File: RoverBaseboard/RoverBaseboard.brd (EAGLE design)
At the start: 87 x 62.9 mm, 61 parts, among them IC3 3.3V, U1 LD29150DT50R, U2 microSD

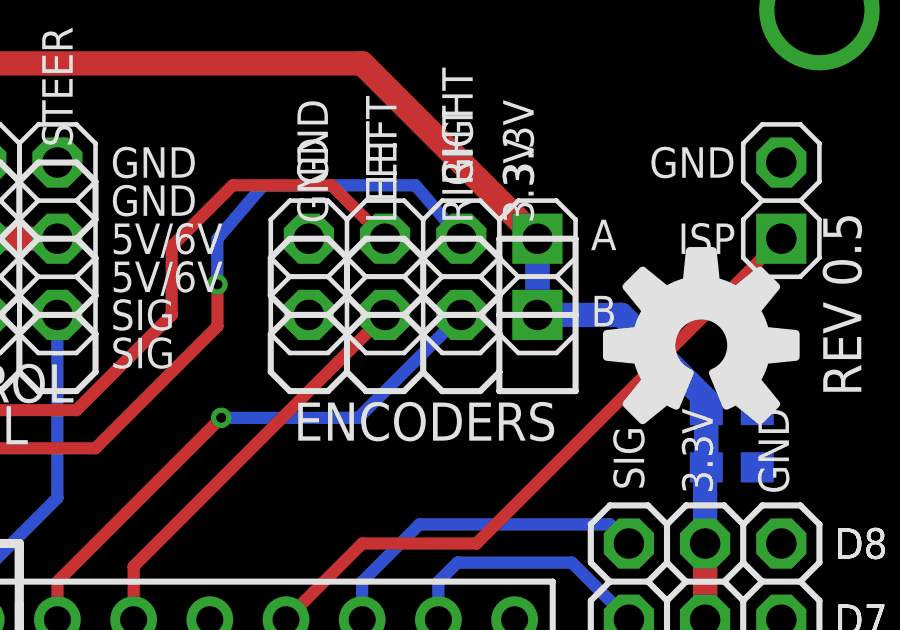
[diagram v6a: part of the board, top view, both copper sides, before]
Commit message: Revised net names to better reflect encoders. Changed pin header labels to better reflect function.
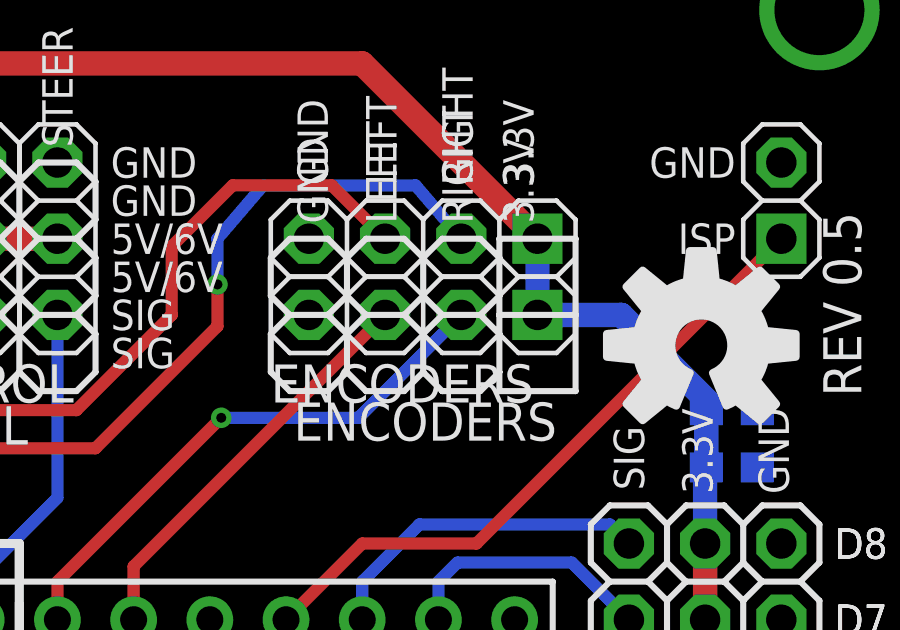
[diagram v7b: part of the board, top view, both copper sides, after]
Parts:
- JP1: value IO -> D0
- JP10: value PWM -> P1
- JP11: value PWM -> P2
- JP13: value IO -> D1
- JP14: value DIGITAL -> D2
- JP15: value ENCODERS -> A
- JP16: value ADC -> A0
- JP17: value ADC -> A1
- JP18: value ADC -> A2
- JP19: value ADC -> A3
- JP2: value ENCODERS -> B
- JP28: value DIGITAL -> D7
- JP29: value DIGITAL -> D8
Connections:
- net ENC0 renamed ENCA_LEFT
- net ENC1 renamed ENCA_RIGHT
- net ENC2 renamed ENCB_RIGHT
- net ENC3 renamed ENCB_LEFT
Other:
- board text removed: "A"
- board text removed: "B"
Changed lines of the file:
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@@
 <text x="11.938" y="45.339" size="1.27" layer="121" font="vector" ratio="16">I2C</text>
 <text x="7.62" y="20.574" size="1.27" layer="122" font="vector" ratio="16" rot="MR180">microSD</text>
-<text x="76.2" y="51.689" size="1.016" layer="25" font="vector" ratio="10">A</text>
-<text x="76.2" y="49.149" size="1.016" layer="25" font="vector" ratio="10">B</text>
 <text x="77.47" y="11.176" size="1.016" layer="25" ratio="10">ANALOG</text>
 <text x="77.47" y="23.876" size="1.016" layer="25" ratio="10">DIGITAL</text>
@@
 <text x="81.026" y="52.578" size="1.016" layer="25" font="vector" ratio="10" rot="R180">ISP</text>
 <text x="81.026" y="55.118" size="1.016" layer="25" font="vector" ratio="10" rot="R180">GND</text>
+<text x="65.532" y="46.609" size="1.27" layer="25" ratio="10">ENCODERS</text>
 </plain>
 <attributes>
@@
 <attribute name="NAME" x="8.255" y="51.054" size="1.016" layer="26" ratio="10" rot="MR270"/>
 </element>
-<element name="JP15" library="pinhead-2" package="1X04-S" value="ENCODERS" x="70.612" y="52.07" smashed="yes" rot="R180">
+<element name="JP15" library="pinhead-2" package="1X04-S" value="A" x="70.612" y="52.07" smashed="yes" rot="R180">
 <attribute name="OC_NEWARK" value="unknown" x="70.612" y="52.07" size="1.778" layer="27" rot="R180" display="off"/>
 <attribute name="MF" value="" x="70.612" y="52.07" size="1.778" layer="27" rot="R180" display="off"/>
 <attribute name="MPN" value="" x="70.612" y="52.07" size="1.778" layer="27" rot="R180" display="off"/>
+<attribute name="VALUE" x="76.2" y="51.435" size="1.016" layer="27"/>
 </element>
 <element name="JP4" library="pinhead-2" package="1X02-S" value="RST" x="19.05" y="6.35" smashed="yes">
@@
 <attribute name="NAME" x="62.992" y="11.938" size="1.016" layer="26" ratio="10" rot="MR90"/>
 </element>
-<element name="JP2" library="pinhead-2" package="1X04-S" value="ENCODERS" x="70.612" y="49.53" smashed="yes" rot="R180">
+<element name="JP2" library="pinhead-2" package="1X04-S" value="B" x="70.612" y="49.53" smashed="yes" rot="R180">
 <attribute name="OC_NEWARK" value="unknown" x="70.612" y="49.53" size="1.778" layer="27" rot="R180" display="off"/>
 <attribute name="MPN" value="" x="70.612" y="49.53" size="1.778" layer="27" rot="R180" display="off"/>
 <attribute name="MF" value="" x="70.612" y="49.53" size="1.778" layer="27" rot="R180" display="off"/>
-<attribute name="VALUE" x="66.294" y="46.609" size="1.27" layer="27" font="vector" ratio="10"/>
+<attribute name="VALUE" x="76.2" y="48.895" size="1.016" layer="27"/>
 </element>
 <element name="JP5" library="pinhead-2" package="1X03-S" value="RXSPD" x="50.8" y="52.07" smashed="yes" rot="R90">
@@
 <attribute name="VALUE" x="53.594" y="56.388" size="1.016" layer="27" font="vector" ratio="10" rot="R90"/>
 </element>
-<element name="JP10" library="pinhead-2" package="1X03-S" value="PWM" x="80.01" y="34.29" smashed="yes">
+<element name="JP10" library="pinhead-2" package="1X03-S" value="P1" x="80.01" y="34.29" smashed="yes">
 <attribute name="OC_NEWARK" value="unknown" x="80.01" y="34.29" size="1.778" layer="27" display="off"/>
 <attribute name="MPN" value="" x="80.01" y="34.29" size="1.778" layer="27" display="off"/>
 <attribute name="MF" value="" x="80.01" y="34.29" size="1.778" layer="27" display="off"/>
 </element>
-<element name="JP11" library="pinhead-2" package="1X03-S" value="PWM" x="80.01" y="36.83" smashed="yes">
+<element name="JP11" library="pinhead-2" package="1X03-S" value="P2" x="80.01" y="36.83" smashed="yes">
 <attribute name="OC_NEWARK" value="unknown" x="80.01" y="36.83" size="1.778" layer="27" display="off"/>
 <attribute name="MPN" value="" x="80.01" y="36.83" size="1.778" layer="27" display="off"/>
 <attribute name="MF" value="" x="80.01" y="36.83" size="1.778" layer="27" display="off"/>
 </element>
-<element name="JP1" library="pinhead-2" package="1X03-S" value="IO" x="80.01" y="31.75" smashed="yes">
+<element name="JP1" library="pinhead-2" package="1X03-S" value="D0" x="80.01" y="31.75" smashed="yes">
 <attribute name="OC_NEWARK" value="unknown" x="80.01" y="31.75" size="1.016" layer="27" font="vector" ratio="12" display="off"/>
 <attribute name="MPN" value="" x="80.01" y="31.75" size="1.016" layer="27" font="vector" ratio="12" display="off"/>
 <attribute name="MF" value="" x="80.01" y="31.75" size="1.016" layer="27" font="vector" ratio="12" display="off"/>
 </element>
-<element name="JP13" library="pinhead-2" package="1X03-S" value="IO" x="80.01" y="29.21" smashed="yes">
+<element name="JP13" library="pinhead-2" package="1X03-S" value="D1" x="80.01" y="29.21" smashed="yes">
 <attribute name="OC_NEWARK" value="unknown" x="80.01" y="29.21" size="1.016" layer="27" font="vector" ratio="12" display="off"/>
 <attribute name="MPN" value="" x="80.01" y="29.21" size="1.016" layer="27" font="vector" ratio="12" display="off"/>
 <attribute name="MF" value="" x="80.01" y="29.21" size="1.016" layer="27" font="vector" ratio="12" display="off"/>
 </element>
-<element name="JP14" library="pinhead-2" package="1X03-S" value="DIGITAL" x="80.01" y="26.67" smashed="yes">
+<element name="JP14" library="pinhead-2" package="1X03-S" value="D2" x="80.01" y="26.67" smashed="yes">
 <attribute name="OC_NEWARK" value="unknown" x="80.01" y="26.67" size="1.016" layer="27" font="vector" ratio="12" display="off"/>
 <attribute name="MPN" value="" x="80.01" y="26.67" size="1.016" layer="27" font="vector" ratio="12" display="off"/>
@@
 <attribute name="VALUE" x="74.295" y="22.225" size="1.27" layer="21" ratio="10" rot="R90"/>
 </element>
-<element name="JP16" library="pinhead-2" package="1X03-S" value="ADC" x="80.01" y="21.59" smashed="yes">
+<element name="JP16" library="pinhead-2" package="1X03-S" value="A0" x="80.01" y="21.59" smashed="yes">
 <attribute name="OC_NEWARK" value="unknown" x="80.01" y="21.59" size="1.016" layer="27" font="vector" ratio="12" display="off"/>
 <attribute name="MPN" value="" x="80.01" y="21.59" size="1.016" layer="27" font="vector" ratio="12" display="off"/>
 <attribute name="MF" value="" x="80.01" y="21.59" size="1.016" layer="27" font="vector" ratio="12" display="off"/>
 </element>
-<element name="JP17" library="pinhead-2" package="1X03-S" value="ADC" x="80.01" y="19.05" smashed="yes">
+<element name="JP17" library="pinhead-2" package="1X03-S" value="A1" x="80.01" y="19.05" smashed="yes">
 <attribute name="OC_NEWARK" value="unknown" x="80.01" y="19.05" size="1.016" layer="27" font="vector" ratio="12" display="off"/>
 <attribute name="MPN" value="" x="80.01" y="19.05" size="1.016" layer="27" font="vector" ratio="12" display="off"/>
 <attribute name="MF" value="" x="80.01" y="19.05" size="1.016" layer="27" font="vector" ratio="12" display="off"/>
 </element>
-<element name="JP18" library="pinhead-2" package="1X03-S" value="ADC" x="80.01" y="16.51" smashed="yes">
+<element name="JP18" library="pinhead-2" package="1X03-S" value="A2" x="80.01" y="16.51" smashed="yes">
 <attribute name="OC_NEWARK" value="unknown" x="80.01" y="16.51" size="1.016" layer="27" font="vector" ratio="12" display="off"/>
 <attribute name="MPN" value="" x="80.01" y="16.51" size="1.016" layer="27" font="vector" ratio="12" display="off"/>
 <attribute name="MF" value="" x="80.01" y="16.51" size="1.016" layer="27" font="vector" ratio="12" display="off"/>
 </element>
-<element name="JP19" library="pinhead-2" package="1X03-S" value="ADC" x="80.01" y="13.97" smashed="yes">
+<element name="JP19" library="pinhead-2" package="1X03-S" value="A3" x="80.01" y="13.97" smashed="yes">
 <attribute name="OC_NEWARK" value="unknown" x="80.01" y="13.97" size="1.016" layer="27" font="vector" ratio="12" display="off"/>
 <attribute name="MPN" value="" x="80.01" y="13.97" size="1.016" layer="27" font="vector" ratio="12" display="off"/>
 <attribute name="MF" value="" x="80.01" y="13.97" size="1.016" layer="27" font="vector" ratio="12" display="off"/>
 </element>
-<element name="JP28" library="pinhead-2" package="1X03-S" value="DIGITAL" x="80.01" y="39.37" smashed="yes">
+<element name="JP28" library="pinhead-2" package="1X03-S" value="D7" x="80.01" y="39.37" smashed="yes">
 <attribute name="OC_NEWARK" value="unknown" x="80.01" y="39.37" size="1.6764" layer="27" font="vector" ratio="12" display="off"/>
 <attribute name="MPN" value="" x="80.01" y="39.37" size="1.6764" layer="27" font="vector" ratio="12" display="off"/>
 <attribute name="MF" value="" x="80.01" y="39.37" size="1.6764" layer="27" font="vector" ratio="12" display="off"/>
 </element>
-<element name="JP29" library="pinhead-2" package="1X03-S" value="DIGITAL" x="80.01" y="41.91" smashed="yes">
+<element name="JP29" library="pinhead-2" package="1X03-S" value="D8" x="80.01" y="41.91" smashed="yes">
 <attribute name="OC_NEWARK" value="unknown" x="80.01" y="41.91" size="1.6764" layer="27" font="vector" ratio="12" display="off"/>
 <attribute name="MPN" value="" x="80.01" y="41.91" size="1.6764" layer="27" font="vector" ratio="12" display="off"/>
@@
 <wire x1="63.5" y1="6.35" x2="63.5" y2="9.31" width="0.4064" layer="16"/>
 </signal>
-<signal name="ENC2">
+<signal name="ENCB_RIGHT">
 <contactref element="JP2" pad="2"/>
 <contactref element="U$1" pad="J6-48"/>
@@
 <wire x1="68.453" y1="46.101" x2="71.882" y2="49.53" width="0.4064" layer="16"/>
 </signal>
-<signal name="ENC3">
+<signal name="ENCB_LEFT">
 <contactref element="JP2" pad="3"/>
 <contactref element="U$1" pad="J6-49"/>
@@
 <wire x1="66.04" y1="36.918" x2="66.04" y2="39.37" width="0.4064" layer="1"/>
 </signal>
-<signal name="ENC0">
+<signal name="ENCA_LEFT">
 <contactref element="U$1" pad="J6-38"/>
 <wire x1="37.465" y1="46.355" x2="33.02" y2="41.91" width="0.4064" layer="1"/>
@@
 <wire x1="67.564" y1="53.848" x2="69.342" y2="52.07" width="0.4064" layer="1"/>
 </signal>
-<signal name="ENC1">
+<signal name="ENCA_RIGHT">
 <contactref element="U$1" pad="J6-39"/>
 <contactref element="JP15" pad="2"/>

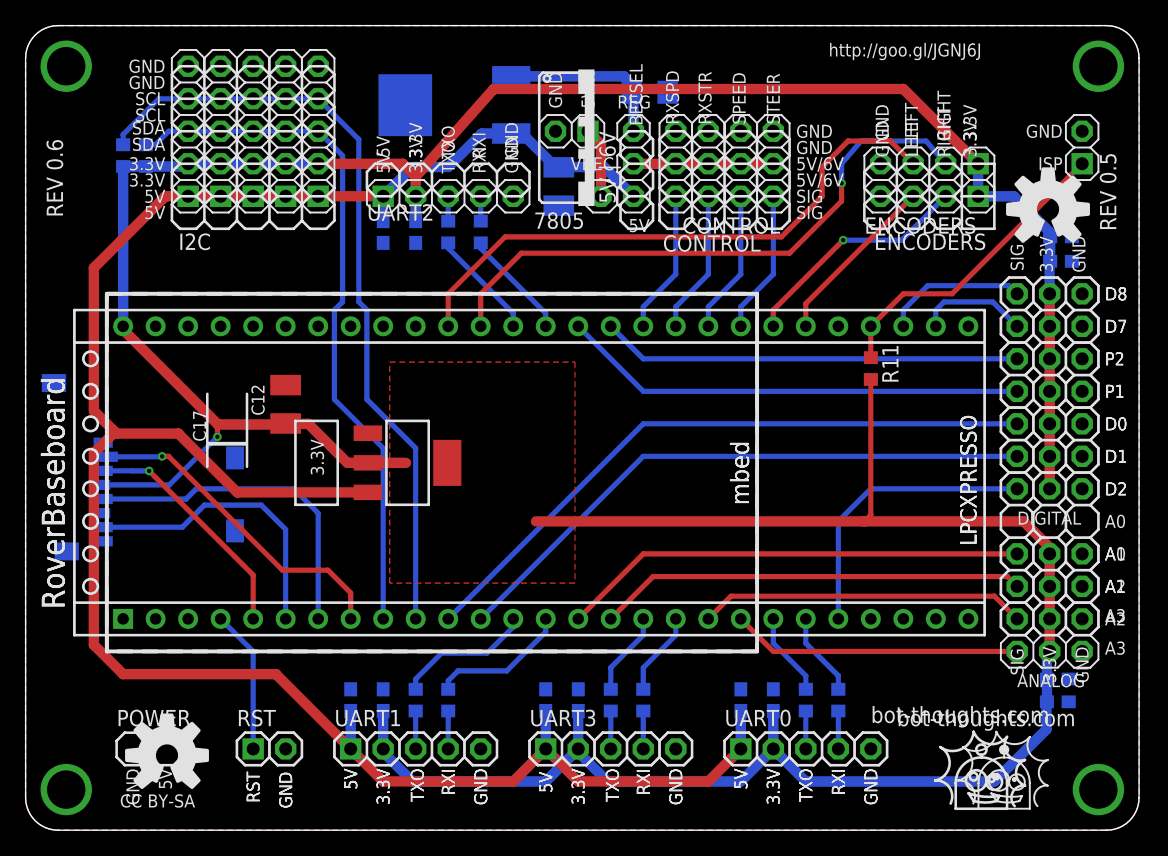
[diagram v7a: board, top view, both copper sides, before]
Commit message: Updated pin names, removed BEC>5V regulator, moved VIN pins back to original spot.
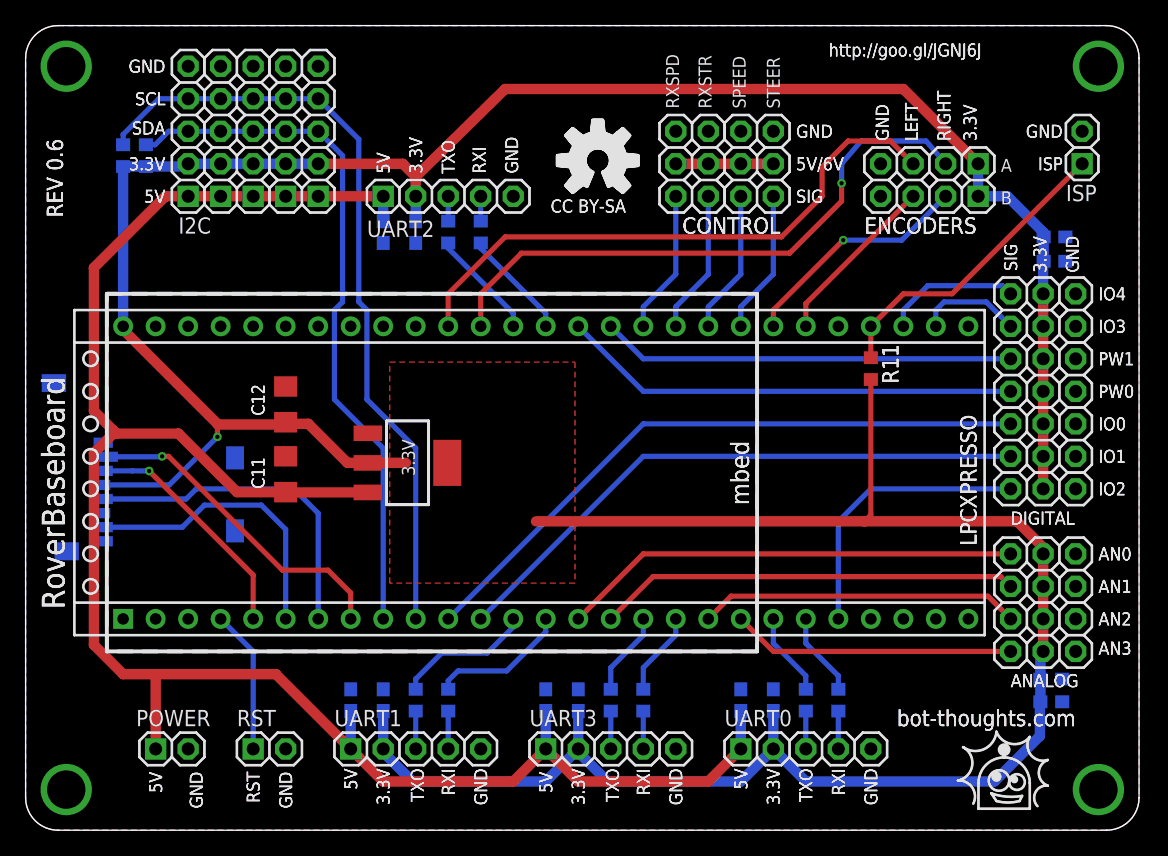
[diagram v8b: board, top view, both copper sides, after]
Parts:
- removed BEC: REG | BYP | 5VIN, pinhead-2:1X03-S
- removed C10: 106, rcl:C1206
- removed JP12: 5VIN, pinhead-2:1X01-S
- removed U1: LD29150DT50R, bt_regulator:DPAK
- C11, C12: value 33uF -> 10uF; device rcl:SMC_B -> rcl:C1206
- JP3: value PWR -> POWER
- moved JP3 57.5 mm to (11.4, 6.35), turned to 0 degrees
- moved C11 31.0 mm to (20.3, 27.8), flipped to the top, turned to 90 degrees
- moved JP1 0.51 mm to (79.5, 31.8)
- moved JP10 0.51 mm to (79.5, 34.3)
- moved JP11 0.51 mm to (79.5, 36.8)
- moved JP13 0.51 mm to (79.5, 29.2)
- moved JP14 0.51 mm to (79.5, 26.7)
- moved JP16 0.51 mm to (79.5, 21.6)
- moved JP17 0.51 mm to (79.5, 19.1)
- moved JP18 0.51 mm to (79.5, 16.5)
- moved JP19 0.51 mm to (79.5, 14.0)
- moved JP28 0.51 mm to (79.5, 39.4)
- moved JP29 0.51 mm to (79.5, 41.9)
- moved C20 0.51 mm to (80.1, 11.8)
- moved C21 0.51 mm to (80.1, 10.0)
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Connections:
- net D0 renamed P11
- net D1 renamed P12
- removed net 5VIN: JP12.1, JP3.1
- removed net 6-7V: BEC.1, C10.1, U1.1
- net +3V3: now also C12.1; no longer C12.+
- net +5V: now also C11.1, JP3.1; no longer BEC.3, C11.+, U1.3
- net BEC: no longer BEC.2
- net GND: now also C11.2, C12.2; no longer C10.2, C11.-, C12.-, U1.4
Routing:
- net +5V: track 170.1 -> 152.4 mm
- net 6-7V: track 13.6 -> 0.00 mm
- net 5VIN: track 5.50 -> 0.00 mm
- net BEC: track 10.9 -> 7.62 mm
- net +3V3: track 291.2 -> 289.8 mm
- net PWM2: track 32.8 -> 32.3 mm
- net PWM1: track 36.4 -> 35.9 mm
- net P12: track 47.2 -> 46.7 mm
- net P11: track 50.8 -> 50.3 mm
- net D8: track 11.2 -> 10.7 mm
- net D7: track 8.67 -> 8.16 mm
- net D2: track 22.6 -> 22.1 mm
- net A3: track 22.6 -> 22.1 mm
- net A2: track 25.6 -> 25.1 mm
- net A1: track 33.4 -> 32.9 mm
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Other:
- board text added: "A"
- board text added: "AN0"
- board text added: "AN1"
- board text added: "AN2"
- board text added: "AN3"
- board text added: "B"
- board text added: "C20"
- board text added: "C21"
- board text added: "C30"
- board text added: "C31"
- board text added: "C40"
- board text added: "C41"
- board text added: "C42"
- board text added: "C43"
- board text added: "C44"
- board text added: "C45"
- board text added: "C46\"
- board text added: "C47"
- board text added: "IO0"
- board text added: "IO1"
- board text added: "IO2"
- board text added: "IO3"
- board text added: "IO4"
- board text added: "PW0"
- board text added: "PW1"
- board text added: "R11"
- board text removed: "5V | 6V"
- board text removed: "5VIN"
- board text removed: "7805"
- board text removed: "A0"
- board text removed: "A1"
- board text removed: "A2"
- board text removed: "A3"
- board text removed: "BECSEL"
- board text removed: "C1"
- board text removed: "C10"
- board text removed: "C13"
- board text removed: "C14"
- board text removed: "C15"
- board text removed: "C16"
- board text removed: "C17"
- board text removed: "C2"
- board text removed: "C3"
- board text removed: "C4"
- board text removed: "C5"
- board text removed: "C6"
- board text removed: "C7"
- board text removed: "C8"
- board text removed: "C9"
- board text removed: "D0"
- board text removed: "D1"
- board text removed: "D2"
- board text removed: "D7"
- board text removed: "D8"
- board text removed: "P1"
- board text removed: "P2"
- board text removed: "REG"
- board text removed: "REV 0.5"
- board text removed: "VBEC"
